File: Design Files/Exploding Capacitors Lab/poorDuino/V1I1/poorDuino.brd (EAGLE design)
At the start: 68.6 x 53.3 mm, 53 parts, among them T1 FDN340P, U1 NCP1117ST50T3G, U2 LP2985-33DBVR, U3 ATMEGA16U2-MU(R), U5 LMV358IDGKR, X1 POWERSUPPLY_DC21MMX, X2 USB-B_TH, Y1 16MHz, Y2 CSTCE16M0V53-R0 16MHZ

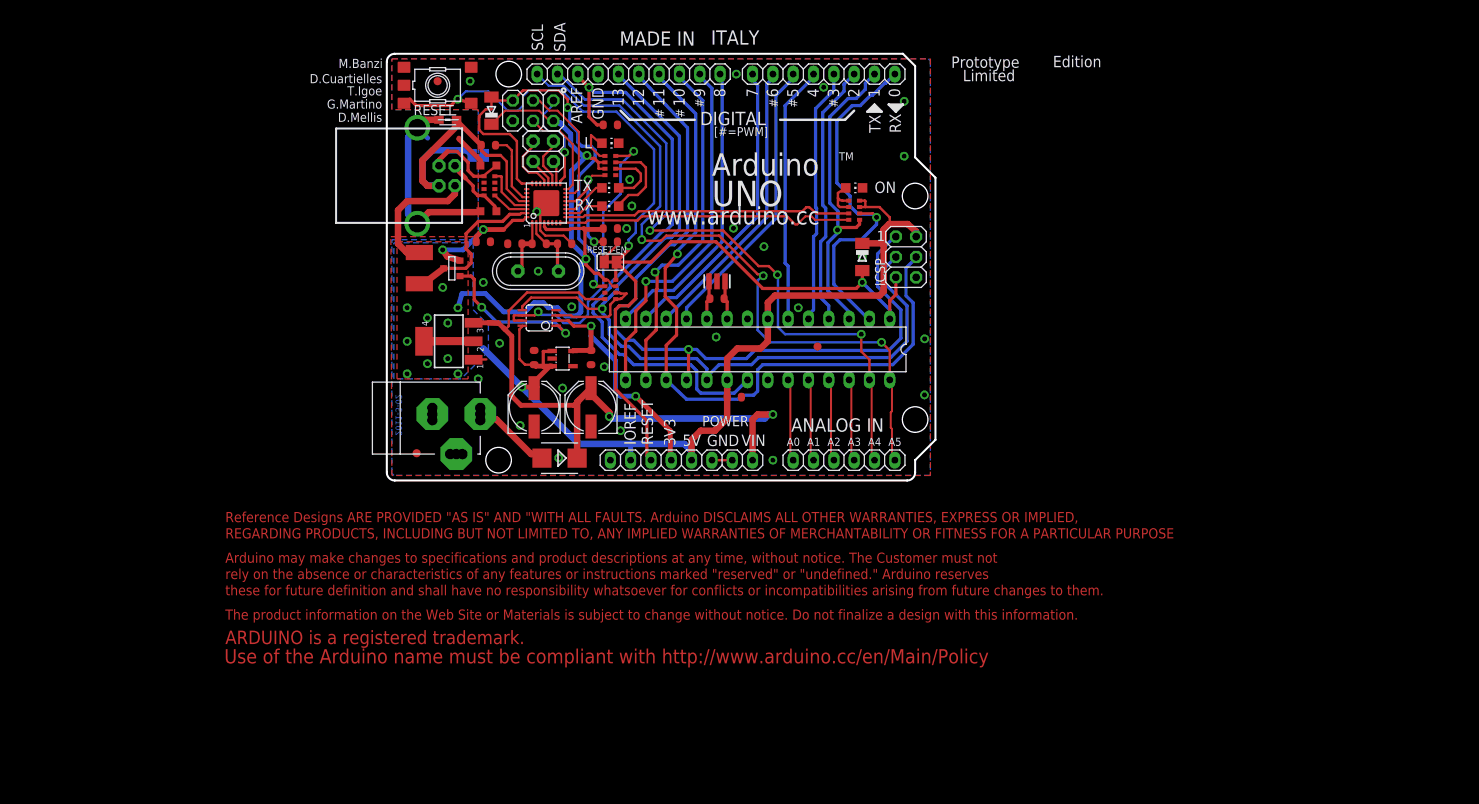
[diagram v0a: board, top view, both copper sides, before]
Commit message: Atmega16U2 with surroundings removed
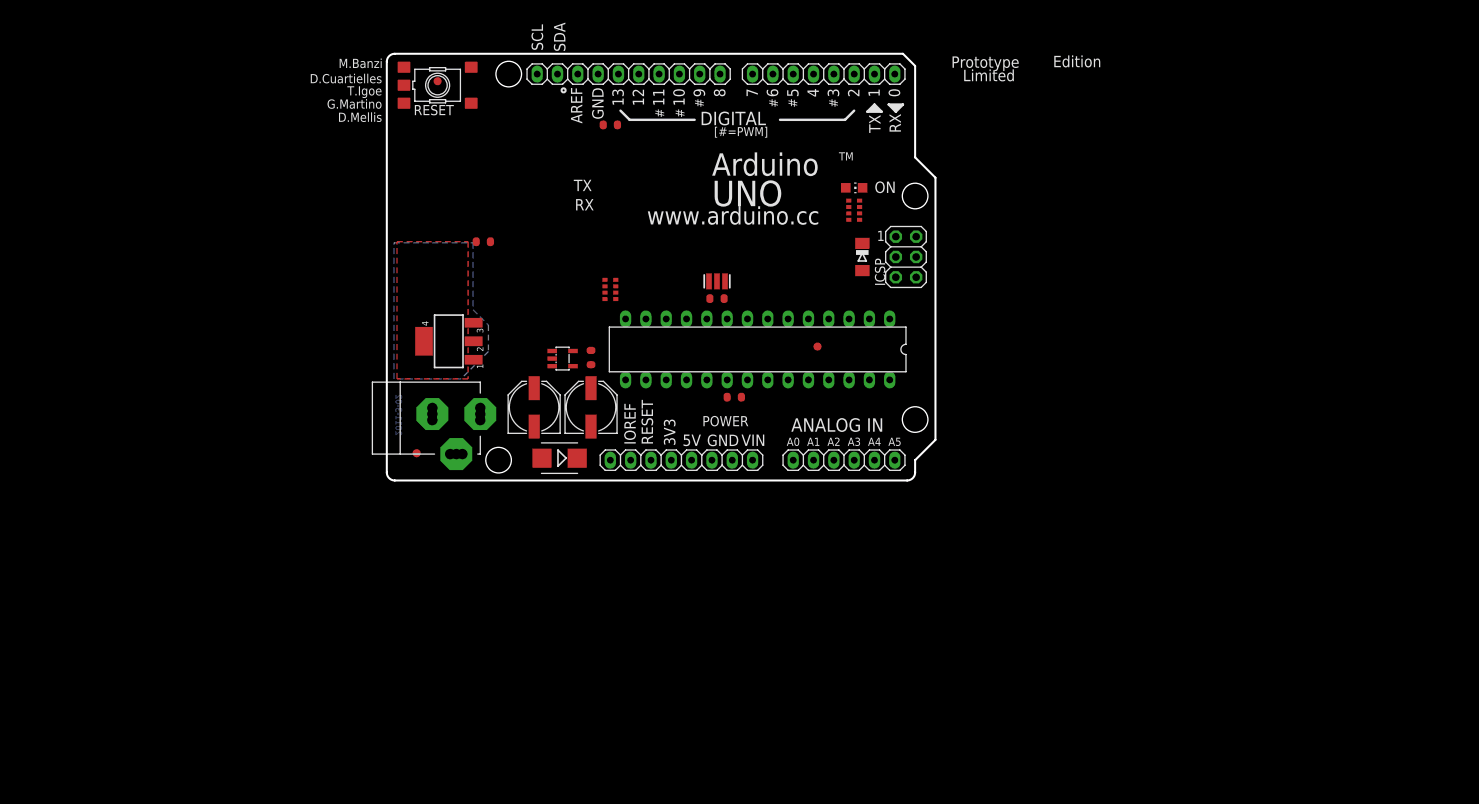
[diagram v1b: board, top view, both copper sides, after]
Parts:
- removed C1, C5, C7: 100n, SmartPrj:C0603-ROUND
- removed C11, C9: 22p, SmartPrj:C0603-ROUND
- removed C8: 1u, SmartPrj:C0603-ROUND
- removed D3: CD1206-S01575, diode:MINIMELF
- removed F1: MF-MSMF050-2 500mA, rcl:L1812
- removed GROUND, RESET-EN: (no value), jumper:SJ
- removed ICSP1: 3x2 M, SmartPrj:2X03
- removed JP2: 2x2 M - NM, SmartPrj:2X02
- removed L, RX, TX: YELLOW, led:CHIP-LED0805
- removed L1: BLM21, wuerth-elektronik:0805
- removed R1: 1M, SmartPrj:R0603-ROUND
- removed RN2: 1K, resistor-dil:CAY16
- removed RN3: 22R, resistor-dil:CAY16
- removed T1: FDN340P, zetex:SOT-23
- removed U$1: DISCLAIMER, SmartPrj:DISCLAIMER
- removed U3: ATMEGA16U2-MU(R), SmartPrj:MLF32
- removed U5: LMV358IDGKR, linear:MSOP08
- removed X2: USB-B_TH, SmartPrj:PN61729
- removed Y1: 16MHz, SmartPrj:QS
- removed Z1, Z2: CG0603MLC-05E, varistor:CT/CN0603
- IOH: device SmartPrj:1X10@1 -> SmartPrj:1X10
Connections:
- removed net CMP: RN1.1, RN1.2, U5.3
- removed net D+: RN3.5, X2.3, Z1.1
- removed net D-: RN3.8, X2.2, Z2.1
- removed net DTR: C5.1, RN2.4, U3.13
- removed net GATE_CMD: T1.3, U5.1
- removed net L13: RN2.8, U5.6, U5.7
- removed net M8RXD: RN4.7, U3.9
- removed net M8TXD: RN4.8, U3.8
- removed net MISO2: ICSP1.1, U3.17
- removed net MOSI2: ICSP1.4, U3.16
- removed net N$1: L.A, RN2.1
- removed net N$35: RN2.7, RX.A
- removed net N$36: RN2.6, TX.A
- removed net PB4: JP2.1, U3.18
- removed net PB5: JP2.3, U3.19
- removed net PB6: JP2.2, U3.20
- removed net PB7: JP2.4, U3.21
- removed net RD+: RN3.4, U3.29
- removed net RD-: RN3.1, U3.30
- removed net RESET2: D3.A, ICSP1.5, RN1.6, U3.24
- removed net RXLED: RX.C, U3.10
- removed net SCK2: ICSP1.3, U3.15
- removed net TP_VUCAP: C8.1, U3.27
- removed net TXLED: TX.C, U3.11
- removed net UGND: C8.2, GROUND.2, L1.1, U3.28, X2.4
- removed net USBVCC: F1.1, T1.1, U3.31
- removed net USHIELD: L1.2, X2.P$1, X2.P$2, Z1.2, Z2.2
- removed net XT1: C9.1, R1.1, U3.1, Y1.2
- removed net XT2: C11.1, R1.2, U3.2, Y1.1
- removed net XUSB: F1.2, X2.1
- net +3V3: no longer U5.2
- net +5V: no longer C1.2, C7.1, D3.C, ICSP1.2, RN1.3, RN2.2, RN2.3, T1.2, U3.32, U3.4, U5.8
- net GND: no longer C1.1, C11.2, C7.2, C9.2, GROUND.1, ICSP1.6, L.C, RN1.7, RN2.5, U3.3, U3.33, U5.4
- net IO0: no longer RN4.2
- net IO1: no longer RN4.1
- net RESET: no longer C5.2, RESET-EN.1, RESET-EN.2
- net SCK: no longer U5.5
- net VIN: no longer RN1.8
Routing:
- net +5V: track 219.6 -> 0.00 mm, vias 15 -> 0
- net RESET: track 141.0 -> 0.00 mm, vias 3 -> 0
- net SCK: track 106.6 -> 0.00 mm, vias 1 -> 0
- net MISO: track 96.7 -> 0.00 mm, vias 1 -> 0
- net MOSI: track 90.8 -> 0.00 mm, vias 1 -> 0
- net AD5/SCL: track 88.1 -> 0.00 mm, vias 3 -> 0
- net VIN: track 81.8 -> 0.00 mm, vias 2 -> 0
- net AD4/SDA: track 81.1 -> 0.00 mm, vias 3 -> 0
- net AREF: track 73.9 -> 0.00 mm, vias 1 -> 0
- net RESET2: track 56.6 -> 0.00 mm, vias 2 -> 0
- net IO0: track 45.6 -> 0.00 mm, vias 1 -> 0
- net IO9: track 45.3 -> 0.00 mm, vias 1 -> 0
- net SS: track 43.8 -> 0.00 mm, vias 1 -> 0
- net IO1: track 39.2 -> 0.00 mm, vias 1 -> 0
- net UGND: track 39.1 -> 0.00 mm
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- removed copper zone on layer 1, net GND
- removed copper zone on layer 16, net GND
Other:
- board text removed: "Use of the Arduino name must be compliant with http://www.arduino.cc/en/Main/Policy"

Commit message: Power supply modification
LDOs, which were originaly in Arduino project, have been replaced to
LD1117xxx.  /schematic only/
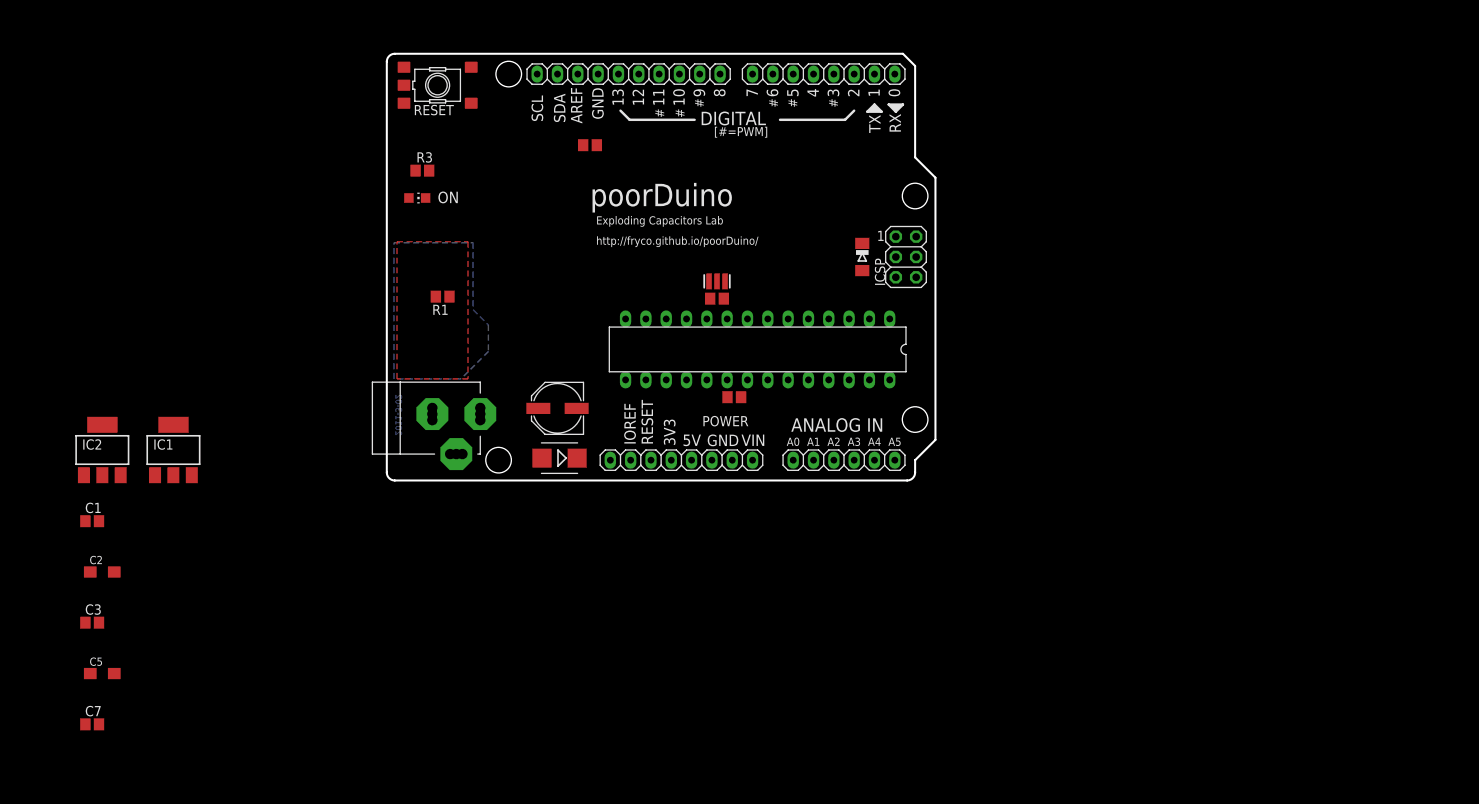
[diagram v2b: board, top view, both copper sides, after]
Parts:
- removed FD1, FD2, FD3: FIDUCIALMOUNT, SmartPrj:FIDUCIA-MOUNT
- removed PC2: 47u, rcl:PANASONIC_D
- removed RN1: 10K, resistor-dil:CAY16
- removed RN4: 1K, resistor-dil:CAY16
- removed U1: NCP1117ST50T3G, linear:SOT223
- removed U2: LP2985-33DBVR, SmartPrj:SOT23-DBV
- added C1, C7: 100n, SmartPrj:C0805
- added C5: 10u, rcl:SMC_A
- added IC1: LD117AS33TR, v-reg:SOT223
- added IC2: LD117AS50TR, v-reg:SOT223
- added R1, R3: 10K, SmartPrj:R0805
- C2: value 100n -> 10u; device SmartPrj:C0603-ROUND -> rcl:SMC_A
- C3: value 1u -> 100n; device SmartPrj:C0603-ROUND -> SmartPrj:C0805
- C4, C6: device SmartPrj:C0603-ROUND -> SmartPrj:C0805
- R2: device SmartPrj:R0603-ROUND -> SmartPrj:R0805
- moved C3 70.6 mm to (-36.8, -17.8), turned to 0 degrees
- moved C2 63.0 mm to (-35.6, -11.4), turned to 0 degrees
- moved ON 54.6 mm to (3.81, 35.3)
- moved PC1 4.19 mm to (21.3, 9.02), turned to 180 degrees
- moved C4 3.59 mm to (25.4, 41.9)
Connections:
- new net VCC: C1.2, C3.2, D1.C, IC1.3, IC2.3
- net +3V3: now also C5.+, IC1.4; no longer C3.2, U2.5
- net +5V: now also C2.+, IC2.4, R1.2, R3.1; no longer C2.2, PC2.+, RN1.5, RN4.3, RN4.4, U1.2, U1.4, U2.1, U2.3
- net AREF: now also C7.2
- net GND: now also C1.1, C2.-, C5.-, C7.1, IC1.1, IC2.1; no longer C2.1, PC2.-, U1.1, U2.2
- net N$3: now also R3.2; no longer RN4.5, RN4.6
- net PWRIN: now also PC1.+
- net RESET: now also R1.1; no longer RN1.4
- net VIN: no longer D1.C, PC1.+, U1.3
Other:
- board text added: "Exploding Capacitors Lab"
- board text added: "http://fryco.github.io/poorDuino/"
- board text added: "poorDuino"
- board text removed: "Arduino"
- board text removed: "D.Cuartielles"
- board text removed: "D.Mellis"
- board text removed: "Edition"
- board text removed: "G.Martino"
- board text removed: "Limited"
- board text removed: "M.Banzi"
- board text removed: "Prototype"
- board text removed: "T.Igoe"
- board text removed: "TM"
- board text removed: "UNO"
- board text removed: "www.arduino.cc"

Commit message: Schematic cleanup
3V3 LED status added
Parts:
- removed C4: 100n, SmartPrj:C0805
- removed D2: CD1206-S01575, diode:MINIMELF
- added 3V3: BLUE, led:CHIP-LED0805
- added R4: 10K, SmartPrj:R0805
- renumbered ON to 5V
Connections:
- new net N$1: 3V3.A, R4.2
- net +3V3: now also R4.1
- net +5V: no longer D2.C
- net AREF: no longer C4.2
- net GND: now also 3V3.C, RESET.3, RESET.4; no longer C4.1, RESET.1, RESET.2
- net RESET: now also RESET.1, RESET.2; no longer D2.A, RESET.3, RESET.4
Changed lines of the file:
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@@
 <attribute name="VALUE" x="20.701" y="11.684" size="1.27" layer="27" ratio="10" rot="R270"/>
 </element>
-<element name="ON" library="led" package="CHIP-LED0805" value="GREEN" x="3.81" y="35.306" smashed="yes" rot="R270">
+<element name="5V" library="led" package="CHIP-LED0805" value="GREEN" x="3.81" y="35.306" smashed="yes" rot="R270">
 <attribute name="NAME" x="6.35" y="34.671" size="1.4224" layer="25" font="vector" ratio="15"/>
 <attribute name="VALUE" x="2.54" y="32.766" size="1.27" layer="27"/>
@@
 <attribute name="VALUE" x="11.176" y="12.319" size="1.778" layer="27" ratio="5" rot="R180"/>
 </element>
-<element name="C4" library="SmartPrj" package="C0805" value="100n" x="25.4" y="41.91" smashed="yes" rot="R180">
-<attribute name="NAME" x="26.67" y="41.529" size="1.27" layer="49" ratio="10"/>
-<attribute name="VALUE" x="28.956" y="44.196" size="1.27" layer="27" rot="R180"/>
-</element>
 <element name="R2" library="SmartPrj" package="R0805" value="1M" x="41.275" y="22.733" smashed="yes" rot="R180">
 <attribute name="NAME" x="40.259" y="20.701" size="1.27" layer="49" ratio="10"/>
@@
 <attribute name="NAME" x="39.4208" y="6.7818" size="1.27" layer="25" ratio="10"/>
 <attribute name="VALUE" x="26.67" y="-0.635" size="1.27" layer="27"/>
-</element>
-<element name="D2" library="diode" package="MINIMELF" value="CD1206-S01575" x="59.436" y="27.94" smashed="yes" rot="R270">
-<attribute name="NAME" x="57.023" y="29.337" size="1.27" layer="49" rot="R270"/>
-<attribute name="VALUE" x="57.023" y="29.591" size="1.27" layer="27" rot="R270"/>
 </element>
 <element name="R1" library="SmartPrj" package="R0805" value="10K" x="6.985" y="22.987" rot="R180"/>
@@
 <element name="C5" library="rcl" package="SMC_A" value="10u" x="-35.56" y="-24.13"/>
 <element name="C7" library="SmartPrj" package="C0805" value="100n" x="-36.83" y="-30.48"/>
+<element name="R4" library="SmartPrj" package="R0805" value="10K" x="-36.83" y="-36.83"/>
+<element name="3V3" library="led" package="CHIP-LED0805" value="BLUE" x="-43.18" y="-36.83"/>
 </elements>
 <signals>
@@
 <contactref element="POWER" pad="5"/>
 <contactref element="POWER" pad="2"/>
-<contactref element="D2" pad="C"/>
 <polygon width="0.3048" layer="16" spacing="0.8128" isolate="0.4064" orphans="yes" thermals="no">
 <vertex x="0.889" y="29.718"/>
@@
 <contactref element="C2" pad="+"/>
 <contactref element="ZU4" pad="7"/>
-<wire x1="59.436" y1="29.64" x2="66.167" y2="30.48" width="0" layer="19" extent="1-1"/>
-<wire x1="47.625" y1="20.193" x2="59.436" y2="29.64" width="0" layer="19" extent="1-1"/>
+<wire x1="47.625" y1="20.193" x2="66.167" y2="30.48" width="0" layer="19" extent="1-1"/>
 <wire x1="42.545" y1="12.573" x2="47.625" y2="20.193" width="0" layer="19" extent="1-1"/>
 <wire x1="42.584" y1="10.414" x2="42.545" y2="12.573" width="0" layer="19" extent="1-1"/>
@@
 <contactref element="PC1" pad="-"/>
 <contactref element="IOH" pad="7"/>
-<contactref element="ON" pad="C"/>
+<contactref element="5V" pad="C"/>
 <contactref element="X1" pad="1"/>
 <contactref element="X1" pad="3"/>
-<contactref element="C4" pad="1"/>
-<contactref element="RESET" pad="2"/>
-<contactref element="RESET" pad="1"/>
 <contactref element="POWER" pad="6"/>
 <contactref element="POWER" pad="7"/>
@@
 <contactref element="C6" pad="1"/>
 <contactref element="C7" pad="1"/>
+<contactref element="RESET" pad="4"/>
+<contactref element="RESET" pad="3"/>
+<contactref element="3V3" pad="C"/>
 <wire x1="45.085" y1="20.193" x2="66.167" y2="25.4" width="0" layer="19" extent="1-1"/>
 <wire x1="41.275" y1="24.892" x2="45.085" y2="20.193" width="0" layer="19" extent="1-1"/>
@@
 <wire x1="8.6868" y1="3.302" x2="23.736" y2="9.017" width="0" layer="19" extent="1-1"/>
 <wire x1="5.6896" y1="8.3058" x2="8.6868" y2="3.302" width="0" layer="19" extent="1-1"/>
-<wire x1="26.25" y1="41.91" x2="41.275" y2="24.892" width="0" layer="19" extent="1-1"/>
-<wire x1="26.416" y1="50.8" x2="26.25" y2="41.91" width="0" layer="19" extent="1-1"/>
-<wire x1="10.55" y1="51.653" x2="26.416" y2="50.8" width="0" layer="19" extent="1-1"/>
-<wire x1="2.15" y1="51.653" x2="10.55" y2="51.653" width="0" layer="19" extent="1-1"/>
-<wire x1="4.86" y1="35.306" x2="2.15" y2="51.653" width="0" layer="19" extent="1-1"/>
+<wire x1="4.86" y1="35.306" x2="5.6896" y2="8.3058" width="0" layer="19" extent="1-1"/>
+<wire x1="2.15" y1="47.153" x2="4.86" y2="35.306" width="0" layer="19" extent="1-1"/>
+<wire x1="10.55" y1="47.153" x2="2.15" y2="47.153" width="0" layer="19" extent="1-1"/>
+<wire x1="26.416" y1="50.8" x2="10.55" y2="47.153" width="0" layer="19" extent="1-1"/>
 <wire x1="-28.97" y1="0.66" x2="5.6896" y2="8.3058" width="0" layer="19" extent="1-1"/>
 <wire x1="-37.86" y1="0.66" x2="-28.97" y2="0.66" width="0" layer="19" extent="1-1"/>
@@
 <wire x1="-34.06" y1="-24.13" x2="-37.68" y2="-17.78" width="0" layer="19" extent="1-1"/>
 <wire x1="-37.68" y1="-30.48" x2="-34.06" y2="-24.13" width="0" layer="19" extent="1-1"/>
+<wire x1="-43.18" y1="-35.78" x2="-37.68" y2="-30.48" width="0" layer="19" extent="1-1"/>
 </signal>
 <signal name="AREF" class="4">
 <contactref element="ZU4" pad="21"/>
 <contactref element="IOH" pad="8"/>
-<contactref element="C4" pad="2"/>
 <contactref element="C7" pad="2"/>
-<wire x1="24.55" y1="41.91" x2="23.876" y2="50.8" width="0" layer="19" extent="1-1"/>
-<wire x1="45.085" y1="12.573" x2="24.55" y2="41.91" width="0" layer="19" extent="1-1"/>
+<wire x1="45.085" y1="12.573" x2="23.876" y2="50.8" width="0" layer="19" extent="1-1"/>
 <wire x1="-35.98" y1="-30.48" x2="45.085" y2="12.573" width="0" layer="19" extent="1-1"/>
 </signal>
 <signal name="RESET">
+<contactref element="POWER" pad="3"/>
+<contactref element="RESET" pad="2"/>
+<contactref element="RESET" pad="1"/>
+<contactref element="R1" pad="1"/>
+<contactref element="ZU4" pad="1"/>
 <contactref element="ICSP" pad="5"/>
-<contactref element="ZU4" pad="1"/>
-<contactref element="RESET" pad="4"/>
-<contactref element="RESET" pad="3"/>
-<contactref element="POWER" pad="3"/>
-<contactref element="D2" pad="A"/>
-<contactref element="R1" pad="1"/>
-<wire x1="59.436" y1="26.24" x2="63.627" y2="25.4" width="0" layer="19" extent="1-1"/>
 <wire x1="62.865" y1="20.193" x2="63.627" y2="25.4" width="0" layer="19" extent="1-1"/>
 <wire x1="33.02" y1="2.54" x2="62.865" y2="20.193" width="0" layer="19" extent="1-1"/>
 <wire x1="7.835" y1="22.987" x2="33.02" y2="2.54" width="0" layer="19" extent="1-1"/>
-<wire x1="10.55" y1="47.153" x2="7.835" y2="22.987" width="0" layer="19" extent="1-1"/>
-<wire x1="2.15" y1="47.153" x2="10.55" y2="47.153" width="0" layer="19" extent="1-1"/>
+<wire x1="10.55" y1="51.653" x2="7.835" y2="22.987" width="0" layer="19" extent="1-1"/>
+<wire x1="2.15" y1="51.653" x2="10.55" y2="51.653" width="0" layer="19" extent="1-1"/>
 </signal>
 <signal name="VIN" class="1">
@@
 </signal>
 <signal name="N$3">
-<contactref element="ON" pad="A"/>
+<contactref element="5V" pad="A"/>
 <contactref element="R3" pad="2"/>
 <wire x1="2.76" y1="35.306" x2="5.295" y2="38.735" width="0" layer="19" extent="1-1"/>
@@
 <contactref element="IC1" pad="4"/>
 <contactref element="C5" pad="+"/>
+<contactref element="R4" pad="1"/>
+<wire x1="-37.06" y1="-24.13" x2="-37.68" y2="-36.83" width="0" layer="19" extent="1-1"/>
 <wire x1="-26.67" y1="6.96" x2="-37.06" y2="-24.13" width="0" layer="19" extent="1-1"/>
 <wire x1="35.56" y1="2.54" x2="-26.67" y2="6.96" width="0" layer="19" extent="1-1"/>
@@
 <wire x1="23.79" y1="2.794" x2="-24.37" y2="0.66" width="0" layer="19" extent="1-1"/>
 </signal>
+<signal name="N$1">
+<contactref element="R4" pad="2"/>
+<contactref element="3V3" pad="A"/>
+<wire x1="-35.98" y1="-36.83" x2="-43.18" y2="-37.88" width="0" layer="19" extent="1-1"/>
+</signal>
 </signals>

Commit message: First attempt to PCB design
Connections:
- removed net VIN: POWER.8
- net VCC: now also POWER.8
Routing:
- net SCK: track 0.00 -> 69.7 mm
- net MOSI: track 0.00 -> 56.2 mm
- net SS: track 0.00 -> 51.0 mm
- net MISO: track 0.00 -> 47.1 mm
- net IO9: track 0.00 -> 43.6 mm
- net IO7: track 0.00 -> 36.1 mm
- net IO6: track 0.00 -> 36.1 mm
- net IO5: track 0.00 -> 36.1 mm
- net IO8: track 0.00 -> 35.5 mm
- net IO4: track 0.00 -> 31.9 mm
- net IO3: track 0.00 -> 31.9 mm
- net IO2: track 0.00 -> 31.9 mm
- net IO1: track 0.00 -> 31.9 mm
- net IO0: track 0.00 -> 31.9 mm
- net AD4/SDA: track 0.00 -> 10.4 mm
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- removed copper zone on layer 1, net +5V
- removed copper zone on layer 16, net +5V
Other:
- board text added: "V1I1"
- board text removed: "2011-3-02"
